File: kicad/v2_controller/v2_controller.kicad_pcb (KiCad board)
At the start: 2 copper layers, 0 parts

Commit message: [kicad] update v2 controller to use hierarchical labels
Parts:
- added C1: 1uF, Capacitor_SMD:C_0402_1005Metric, F.Cu at (191.6, 57.1)
- added C10: 100nF, Capacitor_SMD:C_0402_1005Metric, F.Cu at (191.6, 69.0)
- added C11: 10uF, Capacitor_SMD:C_0603_1608Metric, F.Cu at (159.2, 145.7)
- added C12: 100nF, Capacitor_SMD:C_0402_1005Metric, F.Cu at (162.6, 145.4)
- added C13: 10uF, Capacitor_SMD:C_0603_1608Metric, F.Cu at (159.2, 148.2)
- added C14: 100nF, Capacitor_SMD:C_0402_1005Metric, F.Cu at (162.6, 147.4)
- added C15: 100nF, Capacitor_SMD:C_0402_1005Metric, F.Cu at (162.6, 149.3)
- added C16: 100nF, Capacitor_SMD:C_0402_1005Metric, F.Cu at (162.6, 151.3)
- added C17: 10uF, Capacitor_SMD:C_0603_1608Metric, F.Cu at (159.2, 150.7)
- added C18: 100nF, Capacitor_SMD:C_0402_1005Metric, F.Cu at (162.6, 153.3)
- added C19: 100nF, Capacitor_SMD:C_0402_1005Metric, F.Cu at (170.4, 94.3)
- added C2: 10uF, Capacitor_SMD:C_0603_1608Metric, F.Cu at (192.2, 71.2)
- added C20: 100nF, Capacitor_SMD:C_0402_1005Metric, F.Cu at (170.4, 96.2)
- added C21: 100nF, Capacitor_SMD:C_0402_1005Metric, F.Cu at (170.4, 98.2)
- added C22: 100nF, Capacitor_SMD:C_0402_1005Metric, F.Cu at (170.4, 100.2)
- added C23: 100nF, Capacitor_SMD:C_0402_1005Metric, F.Cu at (170.4, 102.1)
- added C24: 100nF, Capacitor_SMD:C_0402_1005Metric, F.Cu at (170.4, 104.1)
- added C25: 100nF, Capacitor_SMD:C_0402_1005Metric, F.Cu at (170.4, 106.1)
- added C26: 100nF, Capacitor_SMD:C_0402_1005Metric, F.Cu at (173.2, 94.3)
- added C27: 100nF, Capacitor_SMD:C_0402_1005Metric, F.Cu at (173.2, 96.2)
- added C28: 100nF, Capacitor_SMD:C_0402_1005Metric, F.Cu at (173.2, 98.2)
- added C29: 100nF, Capacitor_SMD:C_0402_1005Metric, F.Cu at (173.2, 100.2)
- added C3: 100nF, Capacitor_SMD:C_0402_1005Metric, F.Cu at (191.6, 59.1)
- added C30: 100nF, Capacitor_SMD:C_0402_1005Metric, F.Cu at (173.2, 102.1)
- added C31: 100nF, Capacitor_SMD:C_0402_1005Metric, F.Cu at (173.2, 104.1)
- added C32: 100nF, Capacitor_SMD:C_0402_1005Metric, F.Cu at (173.2, 106.1)
- added C33: 100nF, Capacitor_SMD:C_0402_1005Metric, F.Cu at (176.1, 94.3)
- added C34: 100nF, Capacitor_SMD:C_0402_1005Metric, F.Cu at (176.1, 96.2)
- added C35: 100nF, Capacitor_SMD:C_0402_1005Metric, F.Cu at (176.1, 98.2)
- added C36: 100nF, Capacitor_SMD:C_0402_1005Metric, F.Cu at (176.1, 100.2)
- added C37: 100nF, Capacitor_SMD:C_0402_1005Metric, F.Cu at (176.1, 102.1)
- added C38: 100nF, Capacitor_SMD:C_0402_1005Metric, F.Cu at (176.1, 104.1)
- added C39: 100nF, Capacitor_SMD:C_0402_1005Metric, F.Cu at (176.1, 106.1)
- added C4: 1uF, Capacitor_SMD:C_0402_1005Metric, F.Cu at (191.6, 61.1)
- added C5: 1uF, Capacitor_SMD:C_0402_1005Metric, F.Cu at (191.6, 63.1)
- added C6: 10uF, Capacitor_SMD:C_0603_1608Metric, F.Cu at (192.2, 73.7)
- added C7: 10uF, Capacitor_SMD:C_0603_1608Metric, F.Cu at (192.2, 76.2)
- added C8: 1uF, Capacitor_SMD:C_0402_1005Metric, F.Cu at (191.6, 65.0)
- added C9: 1uF, Capacitor_SMD:C_0402_1005Metric, F.Cu at (191.6, 67.0)
- added D1: SK6812 Mini-E, mantyl:SK6812-MINI-E, F.Cu at (149.4, 95.8)
- added D10: SK6812 Mini-E, mantyl:SK6812-MINI-E, F.Cu at (157.2, 105.0)
- added D11: SK6812 Mini-E, mantyl:SK6812-MINI-E, F.Cu at (157.2, 109.7)
- added D12: SK6812 Mini-E, mantyl:SK6812-MINI-E, F.Cu at (157.2, 114.3)
- added D13: SK6812 Mini-E, mantyl:SK6812-MINI-E, F.Cu at (157.2, 118.9)
- added D14: SK6812 Mini-E, mantyl:SK6812-MINI-E, F.Cu at (157.2, 123.5)
- added D15: SK6812 Mini-E, mantyl:SK6812-MINI-E, F.Cu at (165.0, 95.8)
- added D16: SK6812 Mini-E, mantyl:SK6812-MINI-E, F.Cu at (165.0, 100.4)
- added D17: SK6812 Mini-E, mantyl:SK6812-MINI-E, F.Cu at (165.0, 105.0)
- added D18: 1N5819WS, Diode_SMD:D_SOD-323, F.Cu at (166.2, 152.4)
- added D19: 1N5819WS, Diode_SMD:D_SOD-323, F.Cu at (166.2, 155.3)
- added D2: SK6812 Mini-E, mantyl:SK6812-MINI-E, F.Cu at (149.4, 100.4)
- added D20: Red LED, LED_SMD:LED_0603_1608Metric, F.Cu at (164.1, 143.1)
- added D21: 1N4148WS, Diode_SMD:D_SOD-323, F.Cu at (132.8, 43.9)
- added D22: 1N4148WS, Diode_SMD:D_SOD-323, F.Cu at (132.8, 46.8)
- added D23: 1N4148WS, Diode_SMD:D_SOD-323, F.Cu at (132.8, 49.8)
- added D24: 1N4148WS, Diode_SMD:D_SOD-323, F.Cu at (132.8, 52.7)
- added D25: 1N4148WS, Diode_SMD:D_SOD-323, F.Cu at (132.8, 55.7)
- added D26: 1N4148WS, Diode_SMD:D_SOD-323, F.Cu at (132.8, 58.6)
- added D27: 1N4148WS, Diode_SMD:D_SOD-323, F.Cu at (137.1, 43.9)
- added D28: 1N4148WS, Diode_SMD:D_SOD-323, F.Cu at (137.1, 46.8)
- added D29: 1N4148WS, Diode_SMD:D_SOD-323, F.Cu at (137.1, 49.8)
- added D3: SK6812 Mini-E, mantyl:SK6812-MINI-E, F.Cu at (149.4, 105.0)
- added D30: 1N4148WS, Diode_SMD:D_SOD-323, F.Cu at (137.1, 52.7)
- added D31: 1N4148WS, Diode_SMD:D_SOD-323, F.Cu at (137.1, 55.7)
- added D32: 1N4148WS, Diode_SMD:D_SOD-323, F.Cu at (137.1, 58.6)
- added D33: 1N4148WS, Diode_SMD:D_SOD-323, F.Cu at (141.4, 43.9)
- added D34: 1N4148WS, Diode_SMD:D_SOD-323, F.Cu at (141.4, 46.8)
- added D35: 1N4148WS, Diode_SMD:D_SOD-323, F.Cu at (141.4, 49.8)
- added D36: 1N4148WS, Diode_SMD:D_SOD-323, F.Cu at (141.4, 52.7)
- added D37: 1N4148WS, Diode_SMD:D_SOD-323, F.Cu at (141.4, 55.7)
- added D38: SK6812 Mini-E, mantyl:SK6812-MINI-E, F.Cu at (165.0, 109.7)
- added D39: SK6812 Mini-E, mantyl:SK6812-MINI-E, F.Cu at (165.0, 114.3)
- added D4: SK6812 Mini-E, mantyl:SK6812-MINI-E, F.Cu at (149.4, 109.7)
- added D40: SK6812 Mini-E, mantyl:SK6812-MINI-E, F.Cu at (165.0, 118.9)
- added D41: SK6812 Mini-E, mantyl:SK6812-MINI-E, F.Cu at (165.0, 123.5)
- added D5: SK6812 Mini-E, mantyl:SK6812-MINI-E, F.Cu at (149.4, 114.3)
- added D6: SK6812 Mini-E, mantyl:SK6812-MINI-E, F.Cu at (149.4, 118.9)
- added D7: SK6812 Mini-E, mantyl:SK6812-MINI-E, F.Cu at (149.4, 123.5)
- added D8: SK6812 Mini-E, mantyl:SK6812-MINI-E, F.Cu at (157.2, 95.8)
- added D9: SK6812 Mini-E, mantyl:SK6812-MINI-E, F.Cu at (157.2, 100.4)
- added J1: Conn_02x10_Odd_Even, Connector_IDC:IDC-Header_2x10_P2.54mm_Vertical, F.Cu at (150.8, 62.3)
- added J2: Conn_02x10_Odd_Even, Connector_IDC:IDC-Header_2x10_P2.54mm_Vertical, F.Cu at (162.7, 62.3)
- added J3: USB_C_Receptacle_USB2.0, Connector_USB:USB_C_Receptacle_Molex_105450-0101, F.Cu at (151.3, 132.5)
- added J4: USB_C_Receptacle_USB2.0, Connector_USB:USB_C_Receptacle_Molex_105450-0101, F.Cu at (151.3, 143.0)
- added Q1: S8050, Package_TO_SOT_SMD:SOT-23, F.Cu at (159.6, 137.7)
- added Q2: S8050, Package_TO_SOT_SMD:SOT-23, F.Cu at (159.6, 142.2)
- added R1: 10k, Resistor_SMD:R_0402_1005Metric, F.Cu at (191.8, 43.4)
- added R10: 5.1k, Resistor_SMD:R_0402_1005Metric, F.Cu at (161.5, 128.5)
- added R11: 22.1k, Resistor_SMD:R_0402_1005Metric, F.Cu at (161.5, 130.5)
- added R12: 47.5k, Resistor_SMD:R_0402_1005Metric, F.Cu at (161.5, 132.5)
- added R13: 1k, Resistor_SMD:R_0402_1005Metric, F.Cu at (161.5, 134.5)
- added R14: 10k, Resistor_SMD:R_0402_1005Metric, F.Cu at (164.4, 128.5)
- added R15: 10k, Resistor_SMD:R_0402_1005Metric, F.Cu at (164.4, 130.5)
- added R16: 0, Resistor_SMD:R_0402_1005Metric, F.Cu at (164.4, 132.5)
- added R17: 0, Resistor_SMD:R_0402_1005Metric, F.Cu at (164.4, 134.5)
- added R18: 470, Resistor_SMD:R_0402_1005Metric, F.Cu at (170.4, 108.1)
- added R2: 390k, Resistor_SMD:R_0603_1608Metric, F.Cu at (192.2, 78.7)
- added R3: 10k, Resistor_SMD:R_0402_1005Metric, F.Cu at (191.8, 45.4)
- added R4: 4.7k, Resistor_SMD:R_0402_1005Metric, F.Cu at (191.8, 47.4)
- added R5: 4.7k, Resistor_SMD:R_0402_1005Metric, F.Cu at (191.8, 49.4)
- added R6: 5.1k, Resistor_SMD:R_0402_1005Metric, F.Cu at (158.6, 128.5)
- added R7: 5.1k, Resistor_SMD:R_0402_1005Metric, F.Cu at (158.6, 130.5)
- added R8: 5.1k, Resistor_SMD:R_0402_1005Metric, F.Cu at (158.6, 132.5)
- added R9: 5.1k, Resistor_SMD:R_0402_1005Metric, F.Cu at (158.6, 134.5)
- added SW1: ~, mantyl:Kailh_socket_MX_platemount, F.Cu at (87.2, 50.5)
- added SW10: ~, mantyl:Kailh_socket_MX_platemount, F.Cu at (104.8, 98.9)
- added SW11: ~, mantyl:Kailh_socket_MX_platemount, F.Cu at (104.8, 115.1)
- added SW12: ~, mantyl:Kailh_socket_MX_platemount, F.Cu at (104.8, 131.2)
- added SW13: ~, mantyl:Kailh_socket_MX_platemount, F.Cu at (122.5, 50.5)
- added SW14: ~, mantyl:Kailh_socket_MX_platemount, F.Cu at (122.5, 66.6)
- added SW15: ~, mantyl:Kailh_socket_MX_platemount, F.Cu at (122.5, 82.8)
- added SW16: ~, mantyl:Kailh_socket_MX_platemount, F.Cu at (122.5, 98.9)
- added SW17: ~, mantyl:Kailh_socket_MX_platemount, F.Cu at (122.5, 115.1)
- added SW18: SW_MEC_5E, Button_Switch_SMD:SW_Push_1P1T_XKB_TS-1187A, F.Cu at (186.1, 45.7)
- added SW19: SW_MEC_5E, Button_Switch_SMD:SW_Push_1P1T_XKB_TS-1187A, F.Cu at (186.1, 52.4)
- added SW2: ~, mantyl:Kailh_socket_MX_platemount, F.Cu at (87.2, 66.6)
- added SW3: ~, mantyl:Kailh_socket_MX_platemount, F.Cu at (87.2, 82.8)
- added SW4: ~, mantyl:Kailh_socket_MX_platemount, F.Cu at (87.2, 98.9)
- added SW5: ~, mantyl:Kailh_socket_MX_platemount, F.Cu at (87.2, 115.1)
- added SW6: ~, mantyl:Kailh_socket_MX_platemount, F.Cu at (87.2, 131.2)
- added SW7: ~, mantyl:Kailh_socket_MX_platemount, F.Cu at (104.8, 50.5)
- added SW8: ~, mantyl:Kailh_socket_MX_platemount, F.Cu at (104.8, 66.6)
- added SW9: ~, mantyl:Kailh_socket_MX_platemount, F.Cu at (104.8, 82.8)
- added U1: ESP32-S3-WROOM-1-N16R8, Espressif:ESP32-S3-WROOM-1, F.Cu at (179.8, 72.8)
- added U2: SSD1306_I2C, mantyl:SSD1306_OLED-0.91-128x32_Back_Mount, F.Cu at (146.3, 43.1)
- added U3: 74AHCT1G125, Package_TO_SOT_SMD:SOT-353_SC-70-5, F.Cu at (171.6, 85.8)
- added U4: AMS1117-3.3, Package_TO_SOT_SMD:SOT-223-3_TabPin2, F.Cu at (150.4, 152.7)
- added U5: USBLC6-2P6, Package_TO_SOT_SMD:SOT-666, F.Cu at (166.1, 146.0)
- added U6: USBLC6-2P6, Package_TO_SOT_SMD:SOT-666, F.Cu at (166.1, 149.3)
- added U7: CP2102N-Axx-xQFN24, Package_DFN_QFN:QFN-24-1EP_4x4mm_P0.5mm_EP2.6x2.6mm, F.Cu at (165.2, 138.6)
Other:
- board outline added: 3 x 11 mm

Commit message: [kicad] add pcb board outline
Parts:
- added J5: Conn_02x04_Odd_Even, Connector_PinHeader_2.54mm:PinHeader_2x04_P2.54mm_Vertical, F.Cu at (266.4, 56.9)
- R2: value 390k -> 10k; footprint Resistor_SMD:R_0603_1608Metric -> Resistor_SMD:R_0402_1005Metric
- R3: value 10k -> 390k; footprint Resistor_SMD:R_0402_1005Metric -> Resistor_SMD:R_0603_1608Metric
- moved R15 147.6 mm to (277.7, 35.8)
- moved R16 147.6 mm to (277.7, 37.8)
- moved R14 147.6 mm to (277.7, 33.8)
- moved R17 147.6 mm to (277.7, 39.8)
- moved Q1 139.9 mm to (273.7, 56.8)
- moved Q2 139.9 mm to (273.7, 61.2)
- moved U4 107.3 mm to (248.1, 108.3)
- moved U3 103.8 mm to (273.4, 65.4)
- moved R3 103.0 mm to (168.6, 145.8)
- moved D18 96.3 mm to (254.5, 113.9)
- moved D19 96.3 mm to (254.5, 116.8)
- moved U5 92.6 mm to (255.0, 120.3)
- moved U6 92.6 mm to (255.0, 123.5)
- moved C11 92.6 mm to (248.1, 119.9)
- moved C12 92.6 mm to (251.5, 119.6)
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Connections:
- net /ESP32/LED_NUMPAD_DIN_3V3 renamed /ESP32/LED_DIN_3V3
- net /USB/DTR renamed /ESP32/UART_DTR
- net /USB/RTS renamed /ESP32/UART_RTS
- net CHIP_PU renamed /ESP32/CHIP_PU
- net COL0 renamed /ESP32/COL0
- net COL1 renamed /ESP32/COL1
- net COL2 renamed /ESP32/COL2
- net COL3 renamed /ESP32/COL3
- net COL4 renamed /ESP32/COL4
- net COL5 renamed /ESP32/COL5
- net COL6 renamed /ESP32/COL6
- net COL7 renamed /ESP32/COL7
- net COL8 renamed /ESP32/COL8
- net COL9 renamed /ESP32/COL9
- net GPIO0 renamed /ESP32/GPIO0
- net LED_LEFT_DIN renamed /ESP32/LED_LEFT_DIN
- net LED_NUMPAD_DIN renamed /ESP32/LED_NUMPAD_DIN
- net LED_RIGHT_DIN renamed /ESP32/LED_RIGHT_DIN
- net Net-(D18-A) renamed /USB/USB1_VBUS
- net Net-(D19-A) renamed /USB/USB2_VBUS
- net ROW0 renamed /ESP32/ROW0
- net ROW1 renamed /ESP32/ROW1
- net ROW10 renamed /ESP32/ROW10
- net ROW11 renamed /ESP32/ROW11
- net ROW2 renamed /ESP32/ROW2
- net ROW3 renamed /ESP32/ROW3
- net ROW4 renamed /ESP32/ROW4
- net ROW5 renamed /ESP32/ROW5
- net ROW6 renamed /ESP32/ROW6
- net ROW7 renamed /ESP32/ROW7
- net ROW8 renamed /ESP32/ROW8
- net ROW9 renamed /ESP32/ROW9
- net SCL renamed /ESP32/SCL
- net SDA renamed /ESP32/SDA
- net U0RXD renamed /ESP32/UART_RX
- net U0TXD renamed /ESP32/UART_TX
- net USB_D+ renamed /ESP32/USB_D+
- net USB_D- renamed /ESP32/USB_D-
- R2 pad 1: Net-(U2-IREF) -> +3.3V
- R2 pad 2: GND -> /ESP32/OLED_RST
- R3 pad 1: +3.3V -> Net-(U2-IREF)
- R3 pad 2: /ESP32/SSD1306_RST -> GND
- U1 pad 28: /ESP32/SSD1306_RST -> /ESP32/OLED_RST
- U2 pad 9: /ESP32/SSD1306_RST -> /ESP32/OLED_RST
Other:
- board size 3 x 11 mm -> 100 x 116 mm

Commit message: [kicad] work on PCB layout
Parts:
- SW1, SW10, SW11, SW12, SW13, SW14, SW15, SW16, SW17, SW2, SW3, SW4, SW5, SW6, SW7, SW8, SW9: moved to B.Cu
- moved D17 191.6 mm to (61.5, 53.7)
- moved D13 182.3 mm to (61.5, 81.6)
- moved D6 175.6 mm to (61.5, 119.6)
- moved D16 172.2 mm to (80.5, 53.1)
- moved D12 163.8 mm to (80.5, 72.1)
- moved D2 163.4 mm to (80.5, 129.1)
- moved D9 163.3 mm to (80.5, 91.1)
- moved D5 156.1 mm to (80.5, 110.1)
- moved SW17 155.7 mm to (61.5, 48.0), turned to 180 degrees
- moved D15 152.8 mm to (99.5, 53.1)
- moved SW13 152.7 mm to (61.5, 76.5), turned to 180 degrees
- moved D8 144.9 mm to (99.5, 91.1)
- moved D11 144.4 mm to (99.5, 72.1)
- moved D1 138.5 mm to (109.0, 129.1)
- moved D4 138.0 mm to (99.5, 110.1)
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
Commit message: [kicad] more work on v2 controller PCB layout
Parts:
- U2: moved to B.Cu
- moved R15 272.5 mm to (28.5, 146.0)
- moved R14 271.3 mm to (28.5, 141.0)
- moved R1 264.1 mm to (24.5, 103.0)
- moved R4 264.1 mm to (24.5, 105.0)
- moved R5 264.1 mm to (24.5, 107.0)
- moved R17 260.8 mm to (39.5, 146.1)
- moved R16 259.2 mm to (39.5, 140.1)
- moved C1 257.7 mm to (24.5, 90.0)
- moved C3 257.7 mm to (24.5, 92.0)
- moved Q2 254.1 mm to (34.1, 146.1)
- moved Q1 253.7 mm to (34.1, 140.0)
- moved D20 234.2 mm to (35.8, 44.0)
- moved C18 228.1 mm to (23.5, 126.0)
- moved R10 226.7 mm to (31.5, 44.0)
- moved C17 224.2 mm to (23.9, 122.6)
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- renumbered D25 to D21, D34 to D22, D24 to D23, D29 to D24, D33 to D25, D37 to D26, D23 to D27, D32 to D29, D22 to D30, D27 to D31, D31 to D32, D36 to D33, D21 to D34, D26 to D35, D30 to D36, D35 to D37
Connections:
- D21 pad 1: Net-(D25-K) -> Net-(D21-K)
- D22 pad 1: Net-(D34-K) -> Net-(D22-K)
- D23 pad 1: Net-(D24-K) -> Net-(D23-K)
- D24 pad 1: Net-(D29-K) -> Net-(D24-K)
- D25 pad 1: Net-(D33-K) -> Net-(D25-K)
- D26 pad 1: Net-(D37-K) -> Net-(D26-K)
- D27 pad 1: Net-(D23-K) -> Net-(D27-K)
- D29 pad 1: Net-(D32-K) -> Net-(D29-K)
- D30 pad 1: Net-(D22-K) -> Net-(D30-K)
- D31 pad 1: Net-(D27-K) -> Net-(D31-K)
- D32 pad 1: Net-(D31-K) -> Net-(D32-K)
- D33 pad 1: Net-(D36-K) -> Net-(D33-K)
- D34 pad 1: Net-(D21-K) -> Net-(D34-K)
- D35 pad 1: Net-(D26-K) -> Net-(D35-K)
- D36 pad 1: Net-(D30-K) -> Net-(D36-K)
- D37 pad 1: Net-(D35-K) -> Net-(D37-K)
- SW1 pad 1: Net-(D25-K) -> /ESP32/ROW8
- SW1 pad 2: /ESP32/ROW8 -> Net-(D21-K)
- SW10 pad 1: Net-(D22-K) -> /ESP32/ROW2
- SW10 pad 2: /ESP32/ROW2 -> Net-(D30-K)
- SW11 pad 1: Net-(D27-K) -> /ESP32/ROW3
- SW11 pad 2: /ESP32/ROW3 -> Net-(D31-K)
- SW12 pad 1: Net-(D31-K) -> /ESP32/ROW2
- SW12 pad 2: /ESP32/ROW2 -> Net-(D32-K)
- SW13 pad 1: Net-(D36-K) -> /ESP32/ROW3
- SW13 pad 2: /ESP32/ROW3 -> Net-(D33-K)
- SW14 pad 1: Net-(D21-K) -> /ESP32/ROW0
- SW14 pad 2: /ESP32/ROW0 -> Net-(D34-K)
- SW15 pad 1: Net-(D26-K) -> /ESP32/ROW1
- SW15 pad 2: /ESP32/ROW1 -> Net-(D35-K)
- SW16 pad 1: Net-(D30-K) -> /ESP32/ROW0
- SW16 pad 2: /ESP32/ROW0 -> Net-(D36-K)
- SW17 pad 1: Net-(D35-K) -> /ESP32/ROW1
- SW17 pad 2: /ESP32/ROW1 -> Net-(D37-K)
- SW2 pad 1: Net-(D34-K) -> /ESP32/ROW8
- SW2 pad 2: /ESP32/ROW8 -> Net-(D22-K)
- SW3 pad 1: Net-(D24-K) -> /ESP32/ROW6
- SW3 pad 2: /ESP32/ROW6 -> Net-(D23-K)
- SW4 pad 1: Net-(D29-K) -> /ESP32/ROW7
- SW4 pad 2: /ESP32/ROW7 -> Net-(D24-K)
- SW5 pad 1: Net-(D33-K) -> /ESP32/ROW6
- SW5 pad 2: /ESP32/ROW6 -> Net-(D25-K)
- SW6 pad 1: Net-(D37-K) -> /ESP32/ROW7
- SW6 pad 2: /ESP32/ROW7 -> Net-(D26-K)
- SW7 pad 1: Net-(D23-K) -> /ESP32/ROW4
- SW7 pad 2: /ESP32/ROW4 -> Net-(D27-K)
- SW8 pad 1: Net-(D28-K) -> /ESP32/ROW5
- SW8 pad 2: /ESP32/ROW5 -> Net-(D28-K)
- SW9 pad 1: Net-(D32-K) -> /ESP32/ROW4
- SW9 pad 2: /ESP32/ROW4 -> Net-(D29-K)

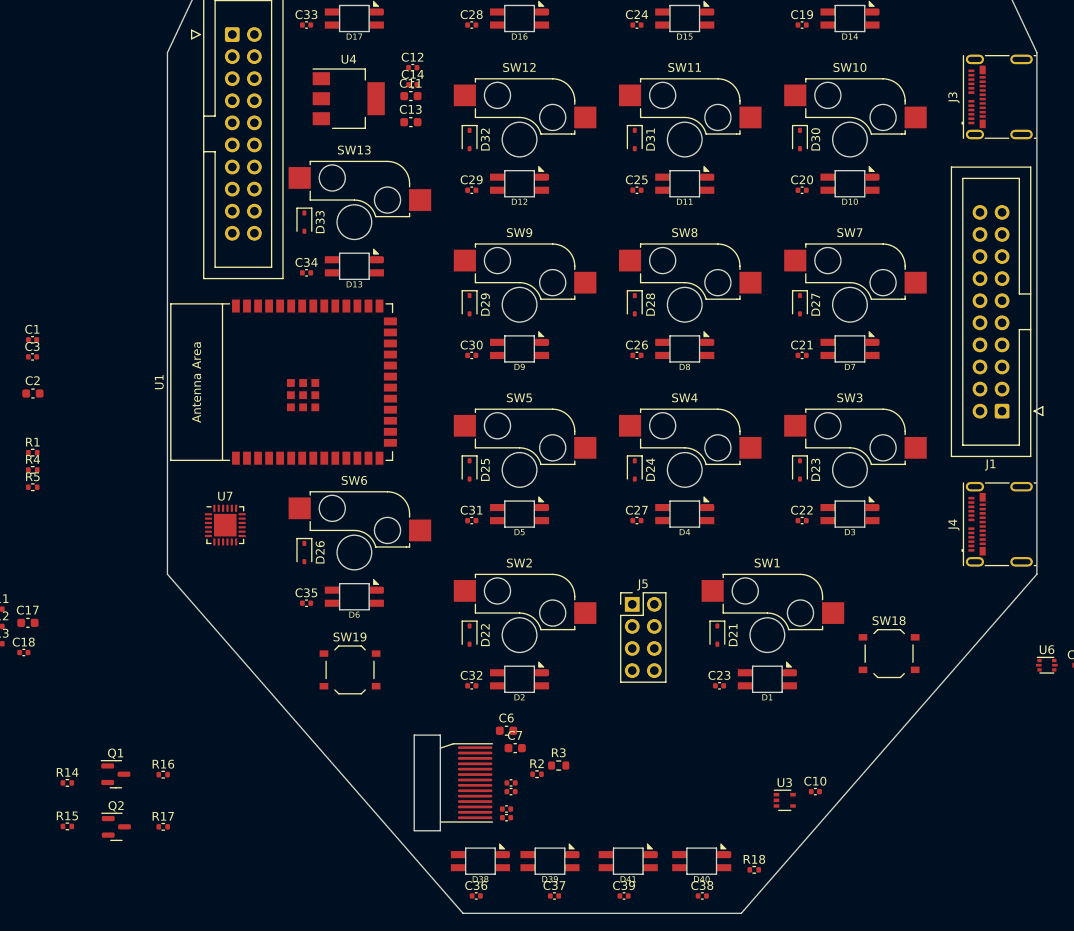
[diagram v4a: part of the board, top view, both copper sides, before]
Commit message: [kicad] more v2 controller work
Update the switch symbols to single pole, since the XKB TS-1187A
footprint only uses 2 pins, even though it has 4 pads.

Also tweak the positioning of the ESP32-S3-WROOM and the board edge,
so that the antenna is off the board.
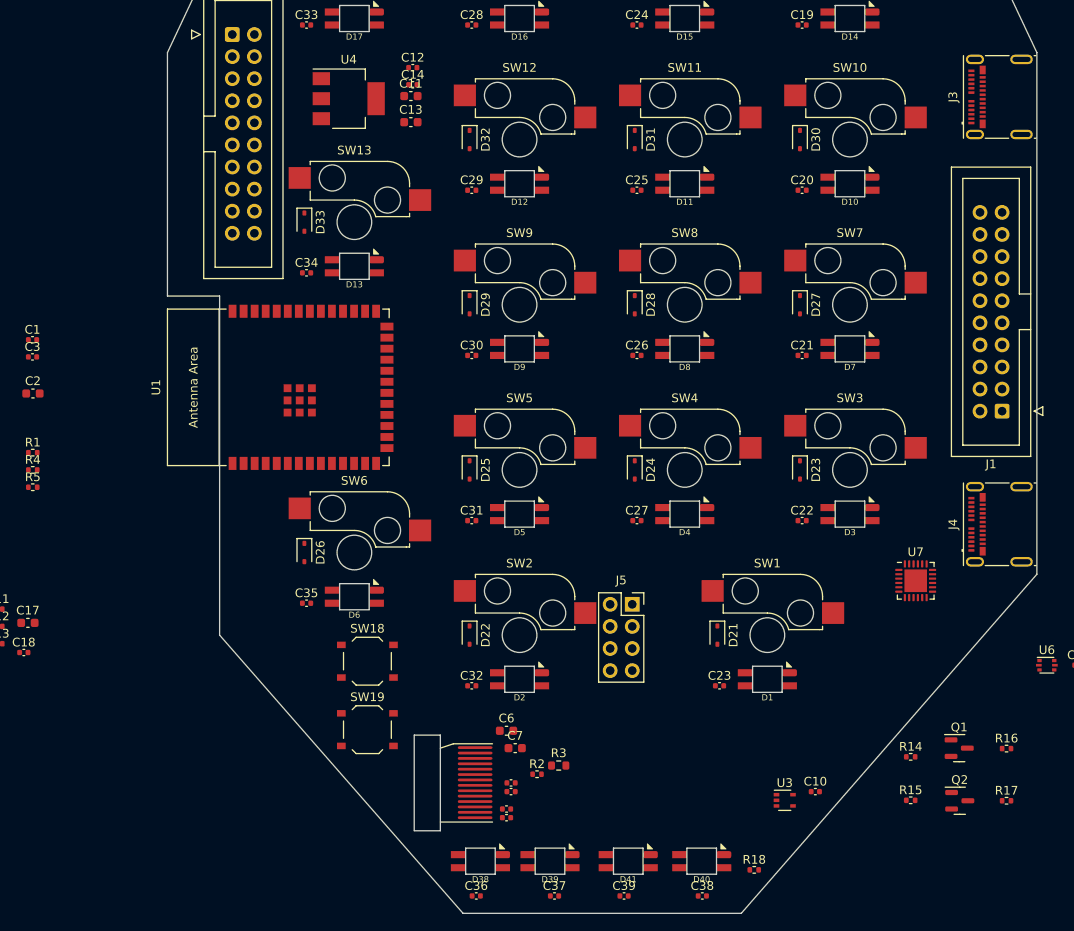
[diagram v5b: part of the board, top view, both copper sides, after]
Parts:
- J5: footprint Connector_PinHeader_2.54mm:PinHeader_2x04_P2.54mm_Vertical -> Connector_PinSocket_2.54mm:PinSocket_2x04_P2.54mm_Vertical
- SW18: value SW_MEC_5E -> Boot
- SW19: value SW_MEC_5E -> Reset
- moved Q1 97.0 mm to (131.1, 137.0)
- moved Q2 97.0 mm to (131.1, 143.1)
- moved R14 97.0 mm to (125.5, 138.0)
- moved R15 97.0 mm to (125.5, 143.0)
- moved R16 97.0 mm to (136.5, 137.1)
- moved R17 97.0 mm to (136.5, 143.1)
- moved U7 79.7 mm to (126.1, 117.8)
- moved SW18 60.0 mm to (63.0, 127.0)
- moved SW19 7.16 mm to (63.0, 134.9)
- moved U1 0.72 mm to (55.8, 95.5)
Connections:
- SW18 pad 2: unconnected-(SW18-Pad2) -> /ESP32/GPIO0
- SW19 pad 2: unconnected-(SW19-Pad2) -> /ESP32/CHIP_PU
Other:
- outline, holes or cut-outs redrawn

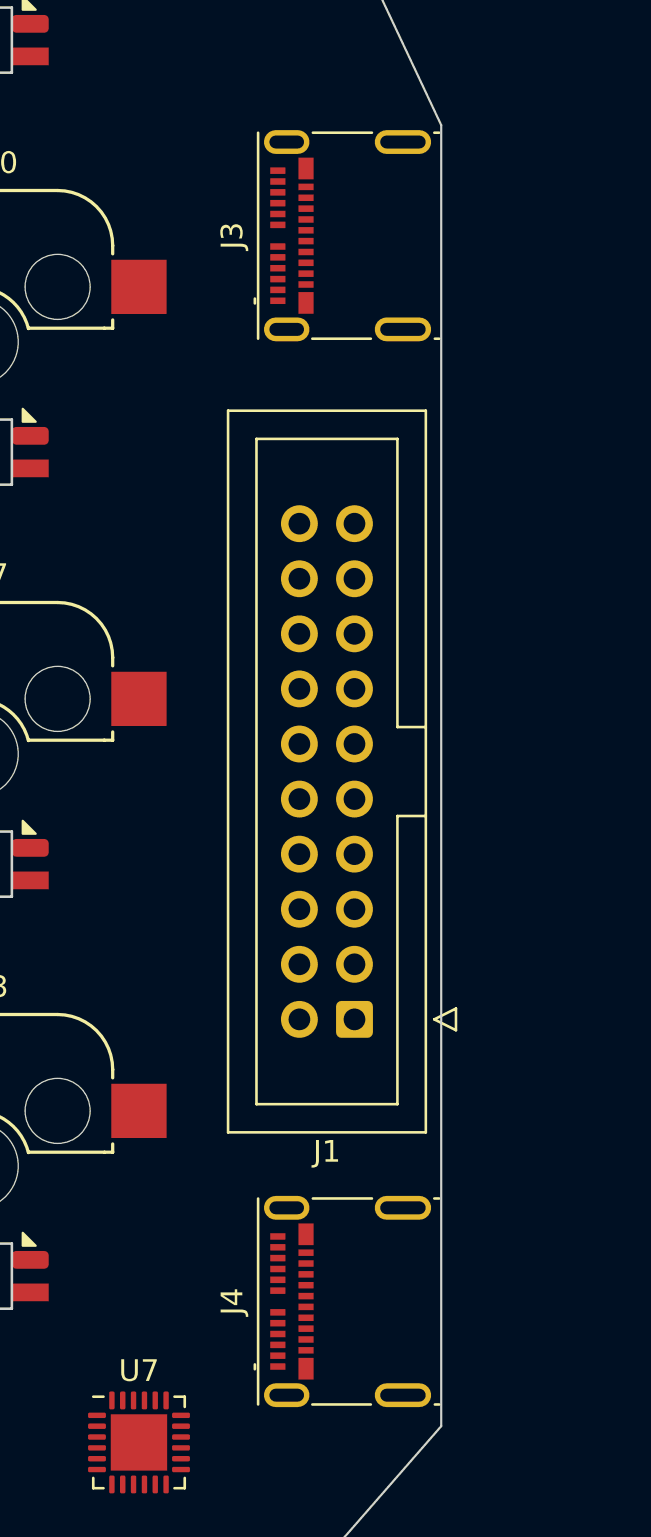
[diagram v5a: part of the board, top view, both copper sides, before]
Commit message: [kicad] use vertical USB-C receptacles
There isn't enough space around the edges of the board for horizontal
mount receptacles.
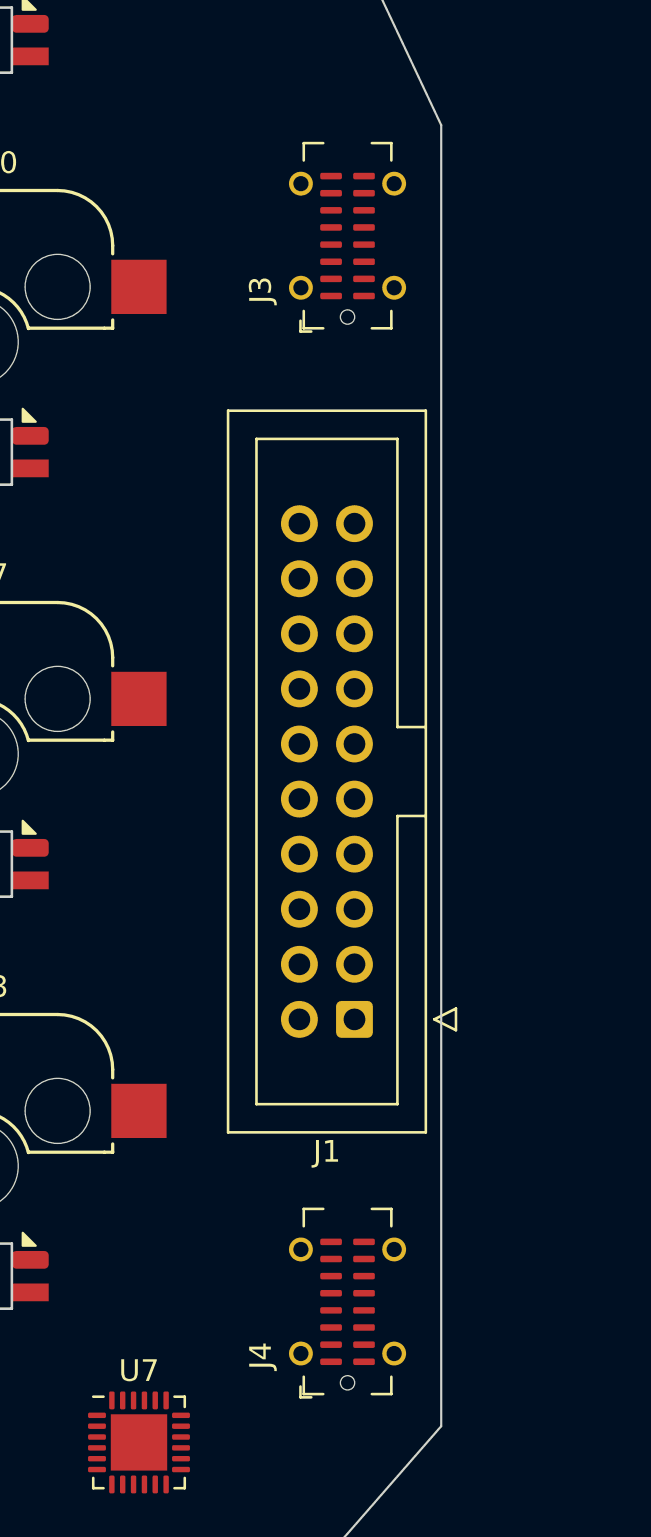
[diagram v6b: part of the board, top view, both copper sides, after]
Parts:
- J3, J4: footprint Connector_USB:USB_C_Receptacle_Molex_105450-0101 -> Connector_USB:USB_C_Receptacle_G-Switch_GT-USB-7051x
